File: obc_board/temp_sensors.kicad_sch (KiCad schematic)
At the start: 34 parts, among them U1 LTC4304IMS#PBF, U2 ADG1607, U3 LT3483ES6, U4 MCP9600-E_MX

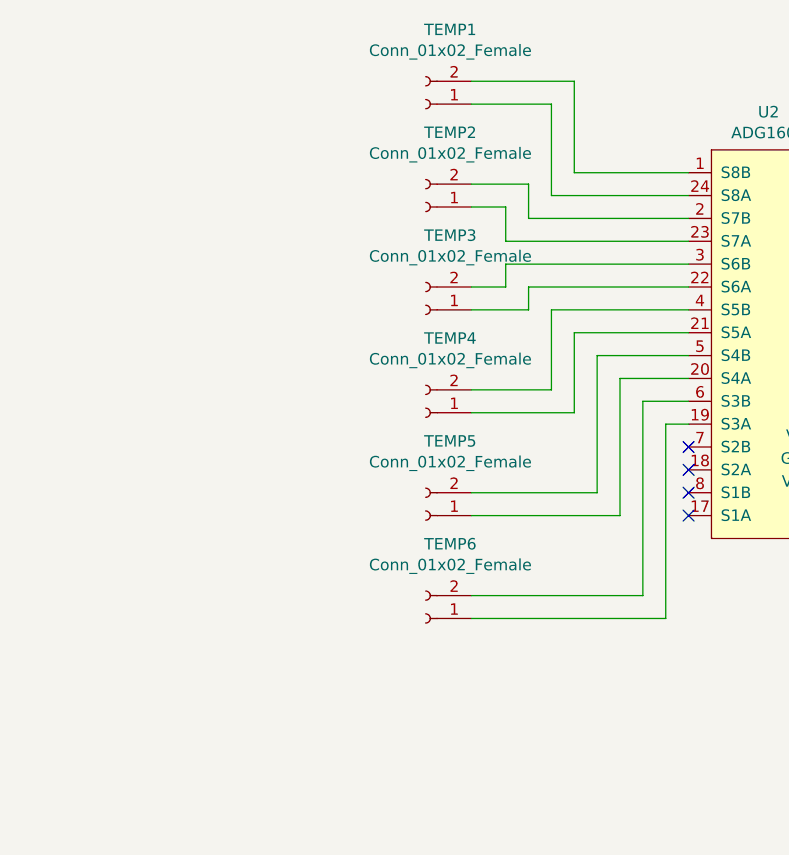
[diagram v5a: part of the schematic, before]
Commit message: changed picoblade symbols to include mounting pins, added photodiode circuitry and additional testpoints, added GPS to FTDI jumper
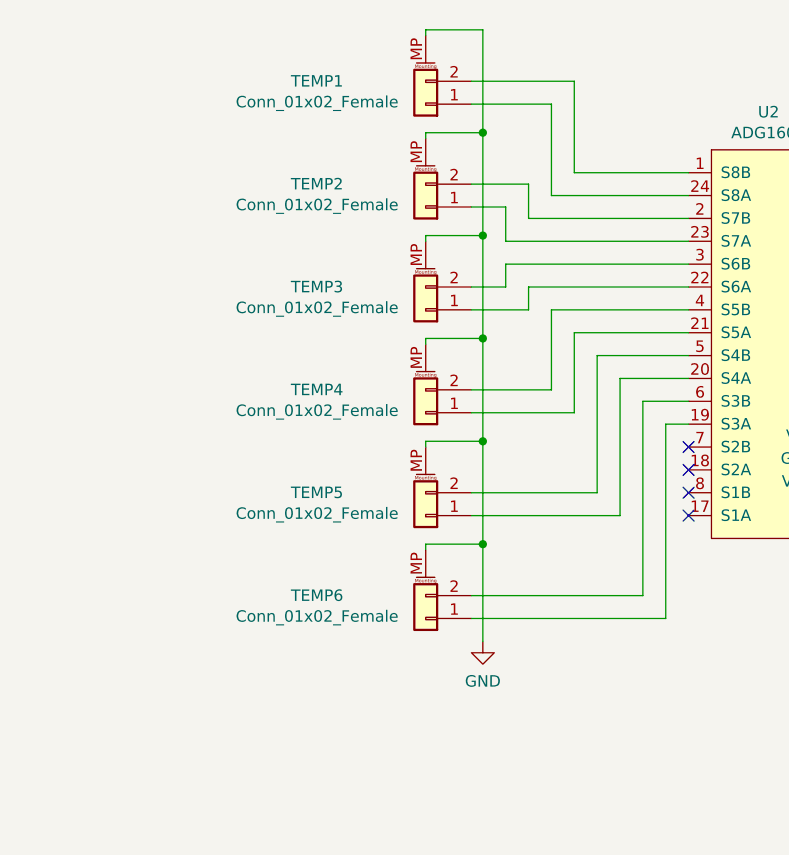
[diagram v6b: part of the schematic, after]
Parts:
- TEMP1, TEMP2, TEMP3, TEMP4, TEMP5, TEMP6: symbol Connector:Conn_01x02_Female -> Connector_Generic_MountingPin:Conn_01x02_MountingPin
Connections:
- net GND: now also TEMP1.MP (MountPin), TEMP2.MP (MountPin), TEMP3.MP (MountPin), TEMP4.MP (MountPin), TEMP5.MP (MountPin), TEMP6.MP (MountPin)

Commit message: v3
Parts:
- added TMP_SCL1, TMP_SDA1: TestPoint, TestPoint:TestPoint_Pad_D1.0mm, symbol Connector:TestPoint
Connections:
- net SCL1: now also TMP_SCL1.1
- net SDA1: now also TMP_SDA1.1
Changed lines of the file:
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@@
+    (stroke (width 0) (type default) (color 0 0 0 0))
+  )
+  (wire (pts (xy 62.23 141.605) (xy 62.23 145.415))
     (stroke (width 0) (type default) (color 0 0 0 0))
   )
   (wire (pts (xy 105.41 58.42) (xy 85.09 58.42))
+    (stroke (width 0) (type default) (color 0 0 0 0))
+  )
+  (wire (pts (xy 76.2 141.605) (xy 76.2 145.415))
     (stroke (width 0) (type default) (color 0 0 0 0))
   )
@@
     (effects (font (size 1.27 1.27)) (justify left))
   )
+  (hierarchical_label "SDA1" (shape input) (at 76.2 145.415 270)
+    (effects (font (size 1.27 1.27)) (justify right))
+  )
   (hierarchical_label "SCL1" (shape input) (at 99.06 184.15 180)
     (effects (font (size 1.27 1.27)) (justify right))
@@
   (hierarchical_label "3V3" (shape input) (at 96.52 168.91 90)
     (effects (font (size 1.27 1.27)) (justify left))
+  )
+  (hierarchical_label "SCL1" (shape input) (at 62.23 145.415 270)
+    (effects (font (size 1.27 1.27)) (justify right))
   )
   (hierarchical_label "MUL_A0" (shape input) (at 123.19 55.88 0)
@@
     (pin "1")
   )
+  (symbol (lib_id "Connector:TestPoint") (at 62.23 141.605 0) (unit 1)
+    (in_bom yes) (on_board yes) (fields_autoplaced)
+    (property "Reference" "TMP_SCL1" (id 0) (at 63.627 137.4683 0)
+      (effects (font (size 1.27 1.27)) (justify left))
+    )
+    (property "Value" "TestPoint" (id 1) (at 63.627 140.0052 0)
+      (effects (font (size 1.27 1.27)) (justify left))
+    )
+    (property "Footprint" "TestPoint:TestPoint_Pad_D1.0mm" (id 2) (at 67.31 141.605 0)
+      (effects (font (size 1.27 1.27)) hide)
+    )
+    (property "Datasheet" "~" (id 3) (at 67.31 141.605 0)
+      (effects (font (size 1.27 1.27)) hide)
+    )
+    (pin "1")
+  )
   (symbol (lib_id "power:GND") (at 187.96 60.96 0) (unit 1)
     (in_bom yes) (on_board yes) (fields_autoplaced)
@@
       (effects (font (size 1.27 1.27)) hide)
     )
+    (pin "1")
+  )
+  (symbol (lib_id "Connector:TestPoint") (at 76.2 141.605 0) (unit 1)
+    (in_bom yes) (on_board yes)
+    (property "Reference" "TMP_SDA1" (id 0) (at 77.597 137.4683 0)
+      (effects (font (size 1.27 1.27)) (justify left))
+    )
+    (property "Value" "TestPoint" (id 1) (at 77.597 140.0052 0)
+      (effects (font (size 1.27 1.27)) (justify left))
+    )
+    (property "Footprint" "TestPoint:TestPoint_Pad_D1.0mm" (id 2) (at 81.28 141.605 0)
+      (effects (font (size 1.27 1.27)) hide)
+    )
+    (property "Datasheet" "~" (id 3) (at 81.28 141.605 0)
+      (effects (font (size 1.27 1.27)) hide)
+    )
